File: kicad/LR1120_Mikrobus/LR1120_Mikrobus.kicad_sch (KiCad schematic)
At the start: 27 parts, among them Q1 NX2016SA-32M-EXS00A-CS06465, Q2 NT2016SA-32M-END4263A, Q3 NX3215SA, U1 LR1120, U2 SKY13588-460LF, U5 LIS2DE12, U7 M24128-BFMH6TG, U8 BGA524N6E6327XTSA1

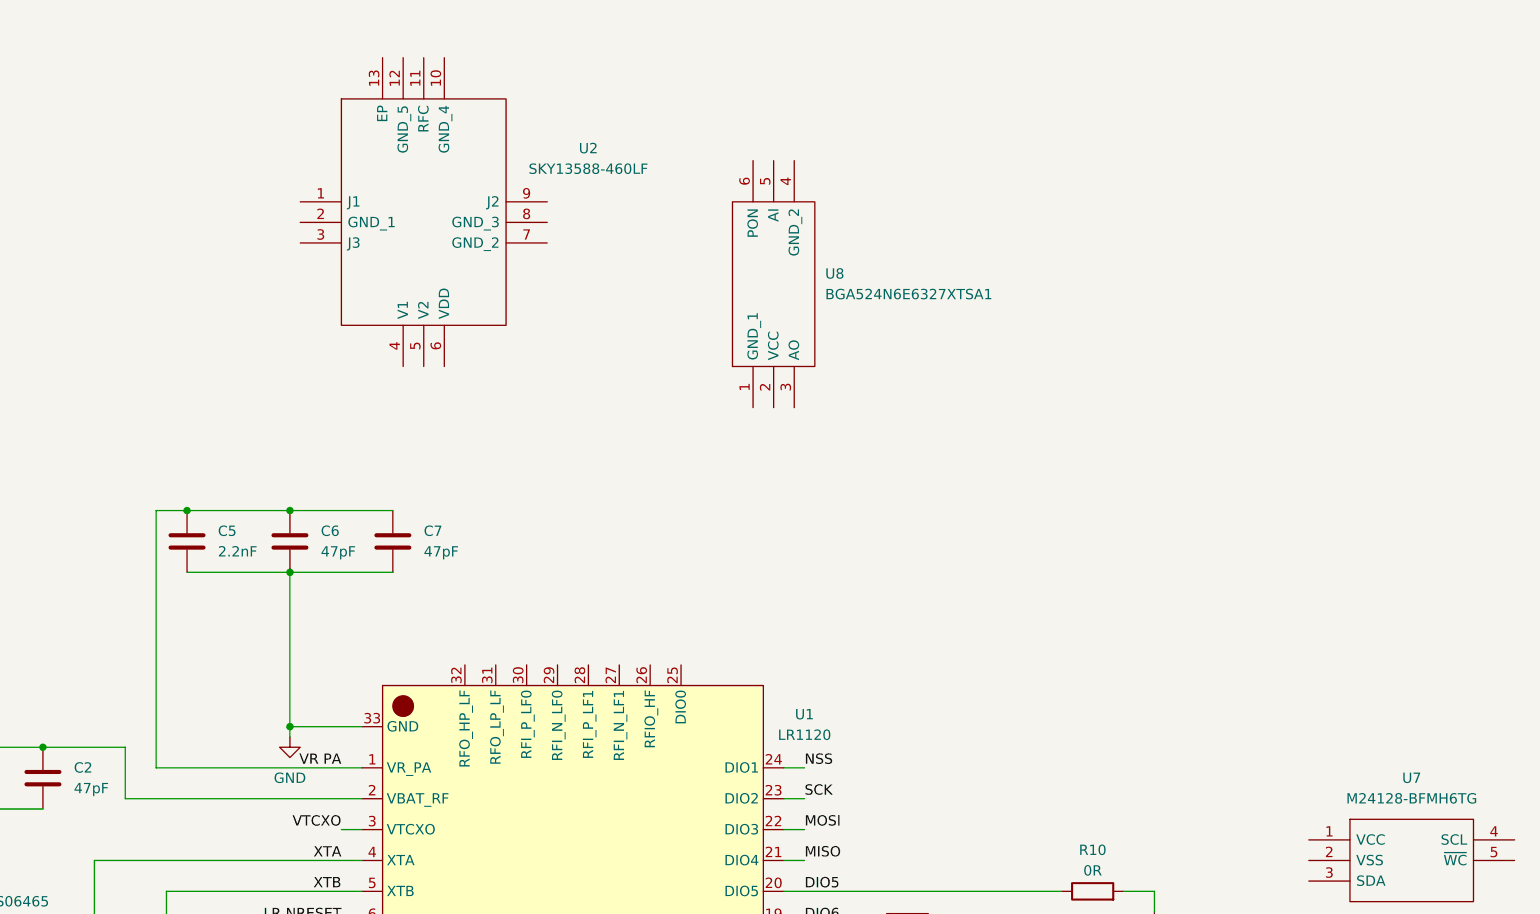
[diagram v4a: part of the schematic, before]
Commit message: added caps, inds and rclamp
Added C22-C26, C27-C28, C30, C53 and C58
Added L11-L13, L15 and L20
Added D3 (rclamp)
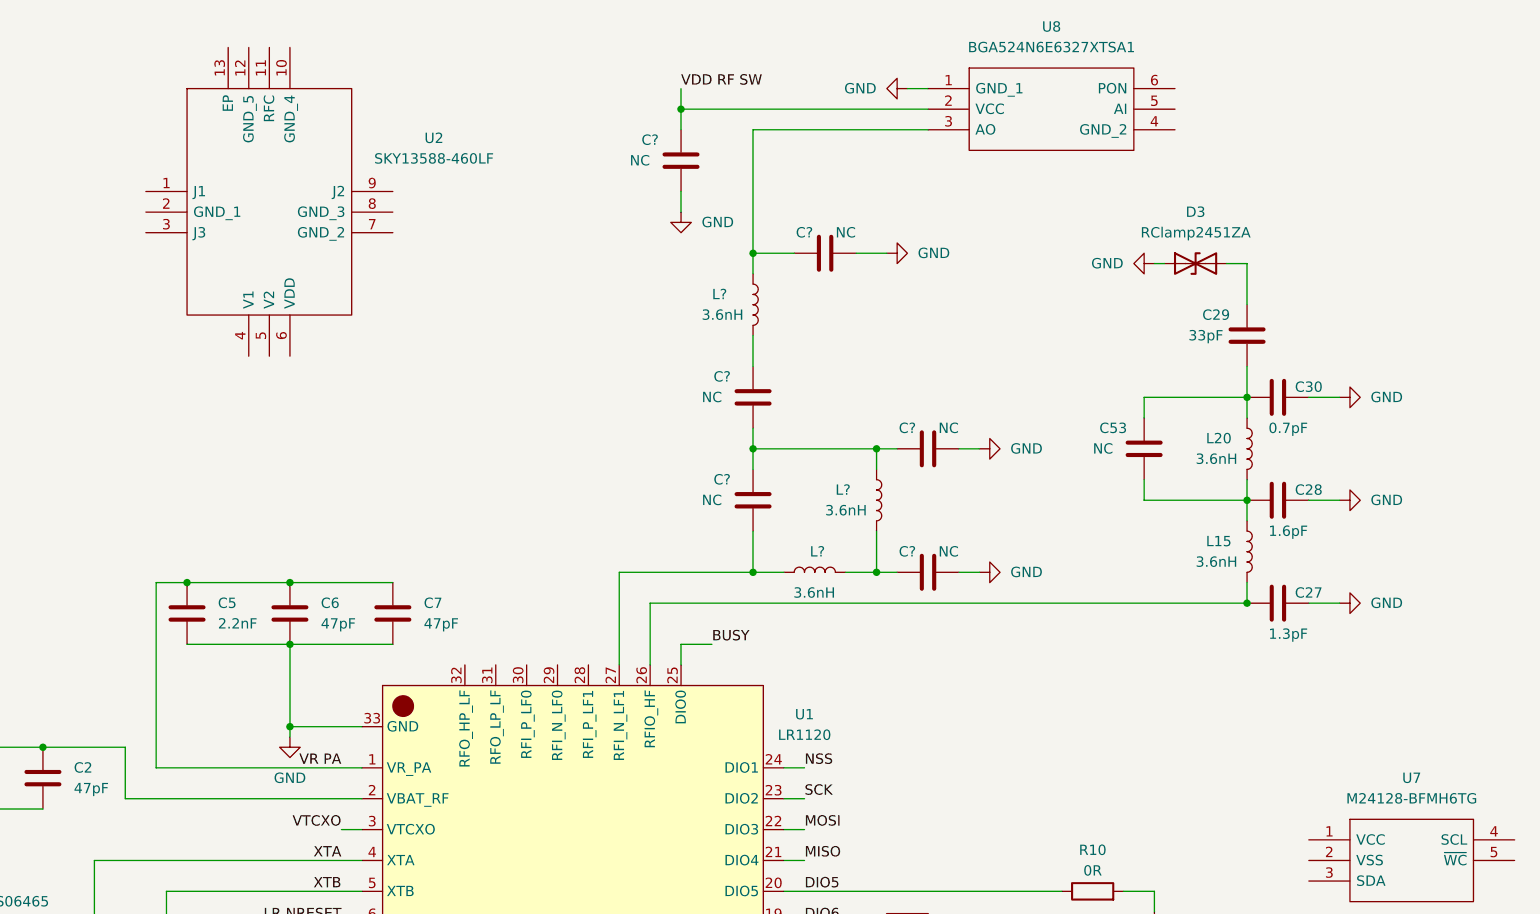
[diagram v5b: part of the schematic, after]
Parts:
- added C27: 1.3pF, Capacitor_SMD:C_01005_0402Metric, symbol Device:C
- added C28: 1.6pF, Capacitor_SMD:C_01005_0402Metric, symbol Device:C
- added C29: 33pF, Capacitor_SMD:C_01005_0402Metric, symbol Device:C
- added C30: 0.7pF, Capacitor_SMD:C_01005_0402Metric, symbol Device:C
- added C53, C? (x6): NC, Capacitor_SMD:C_01005_0402Metric, symbol Device:C
- added D3: RClamp2451ZA, Diode_SMD:D_0201_0603Metric, symbol Device:D_TVS
- added L15, L20, L? (x3): 3.6nH, Inductor_SMD:L_01005_0402Metric, symbol Device:L
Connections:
- net GND: now also U8.1 (GND_1), C27.2, C28.2, C30.2, C?.1, C?.1, C?.1, C?.1, D3.1 (A1)
- net VDD RF SW: now reaches U8.2 (VCC)
- net VDD RF SW: now also C?.2
- net at U8.3 (AO): now also C?.2, L?.1
- net BUSY: now reaches U1.25 (DIO0)
- net at U1.26 (RFIO_HF): now also C27.1, L15.2
- net at U1.27 (RFI_N_LF1): now also C?.1, L?.1
- new net: C28.1, C53.1, L15.1, L20.2
- new net: C29.1, C30.1, C53.2, L20.1
- new net: C?.1, C?.2, C?.2, L?.1
- new net: C?.2, L?.2
- new net: C?.2, L?.2, L?.2
- new net: C29.2, D3.2 (A2)
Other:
- moved on the sheet: C5, C6, C7, U2, U8

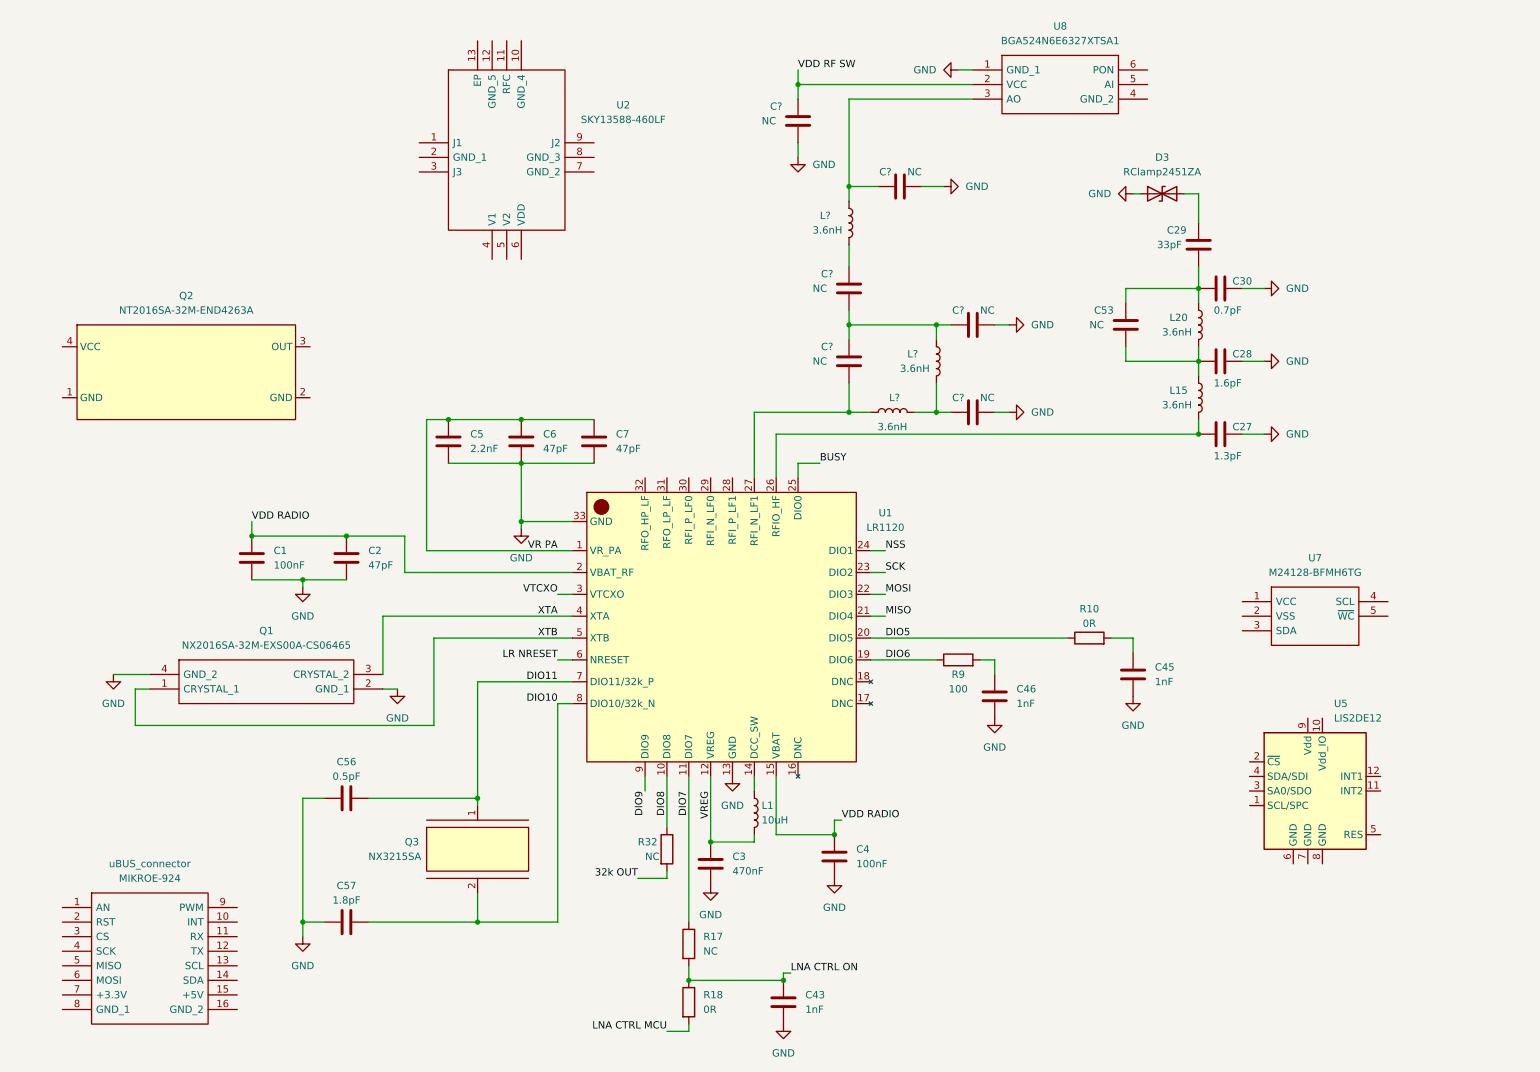
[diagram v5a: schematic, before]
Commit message: Added caps, inds and res
Adeded remaining caps, inds and res, but C47-48, C52 and R31. Some caps, inds and res need be set to the correct footprint and value.
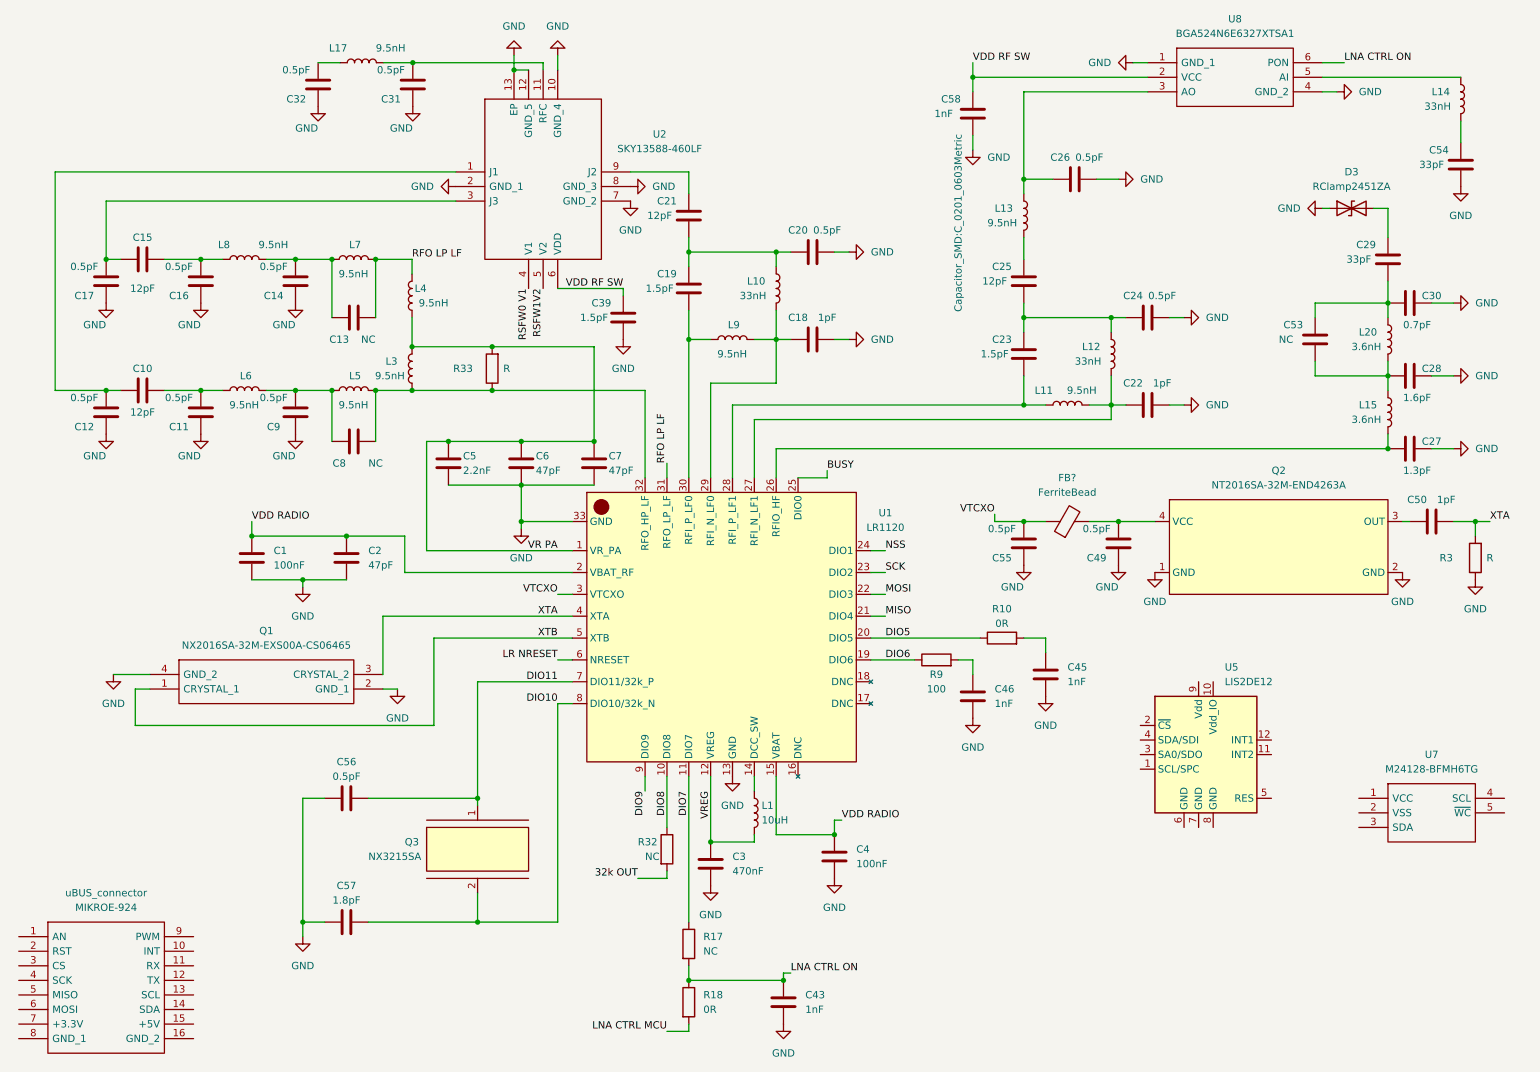
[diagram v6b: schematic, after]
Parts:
- added C10, C15, C21: 12pF, Capacitor_SMD:C_01005_0402Metric, symbol Device:C
- added C11, C12, C14, C16, C17, C20, C31, C32, C49, C55, C9: 0.5pF, Capacitor_SMD:C_01005_0402Metric, symbol Device:C
- added C13, C8: NC, Capacitor_SMD:C_01005_0402Metric, symbol Device:C
- added C18, C50: 1pF, Capacitor_SMD:C_01005_0402Metric, symbol Device:C
- added C19, C39: 1.5pF, Capacitor_SMD:C_01005_0402Metric, symbol Device:C
- added C54: 33pF, Capacitor_SMD:C_01005_0402Metric, symbol Device:C
- added FB?: FerriteBead, symbol Device:FerriteBead
- added L10, L14: 33nH, Inductor_SMD:L_01005_0402Metric, symbol Device:L
- added L17, L3, L4, L5, L6, L7, L8, L9: 9.5nH, Inductor_SMD:L_01005_0402Metric, symbol Device:L
- added R3, R33: R, symbol Device:R
- C22: renamed from C?; value NC -> 1pF
- C23: renamed from C?; value NC -> 1.5pF
- C24, C26: renamed from C?; value NC -> 0.5pF
- C25: renamed from C?; value NC -> 12pF
- C58: renamed from C?; value NC -> 1nF; footprint Capacitor_SMD:C_01005_0402Metric -> Capacitor_SMD:C_0201_0603Metric
- L11, L13: renamed from L?; value 3.6nH -> 9.5nH
- L12: renamed from L?; value 3.6nH -> 33nH
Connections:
- net GND: now also Q2.1 (GND), Q2.2 (GND), U2.10 (GND_4), U2.12 (GND_5), U2.13 (EP), U2.2 (GND_1), U2.7 (GND_2), U2.8 (GND_3), U8.4 (GND_2), C11.2, C12.2, C14.2, C16.2, C17.2, C18.1, C20.1, C31.2, C32.2, C39.1, C49.2, C54.1, C55.2, C9.2, R3.1
- net LNA CTRL ON: now also U8.6 (PON)
- net VDD RF SW: now also U2.6 (VDD), C39.2
- net VR PA: now also L3.2, L4.1, R33.2
- net VTCXO: now also C55.1, FB?.1
- net XTA: now also C50.1, R3.2
- net at U2.1 (J1): now also C10.2, C12.1
- net at U2.11 (RFC): now also C31.1, L17.2
- net at U2.3 (J3): now also C15.2, C17.1
- net RSFW0 V1: now reaches U2.4 (V1)
- net RSFW1V2: now reaches U2.5 (V2)
- net at U2.9 (J2): now also C21.2
- net at U8.5 (AI): now also L14.1
- net at C22.2, L11.2, L12.2: now also U1.27 (RFI_N_LF1)
- net at Q2.3 (OUT): now also C50.2
- net at Q2.4 (VCC): now also C49.1, FB?.2
- net at C23.1, L11.1: now also U1.28 (RFI_P_LF1); no longer U1.27 (RFI_N_LF1)
- net at U1.29 (RFI_N_LF0): now also C18.2, L10.2, L9.2
- net at U1.30 (RFI_P_LF0): now also C19.1, L9.1
- net RFO LP LF: now reaches U1.31 (RFO_LP_LF)
- net RFO LP LF: now also C13.1, L4.2, L7.2
- net at U1.32 (RFO_HP_LF): now also C8.1, L3.1, L5.2, R33.1
- new net: C19.2, C20.2, C21.1, L10.1
- new net: C8.2, C9.1, L5.1, L6.2
- new net: C54.2, L14.2
- new net: C32.1, L17.1
- new net: C15.1, C16.1, L8.1
- new net: C13.2, C14.1, L7.1, L8.2
- new net: C10.1, C11.1, L6.1
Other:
- moved on the sheet: C22, C23, C24, C25, C26, C27, C28, C29, C30, C45, C46, C5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

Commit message: Added all comp, except connectors
Added almost all components. Still remains to be placed the microbus connector and the associated caps, res and switches
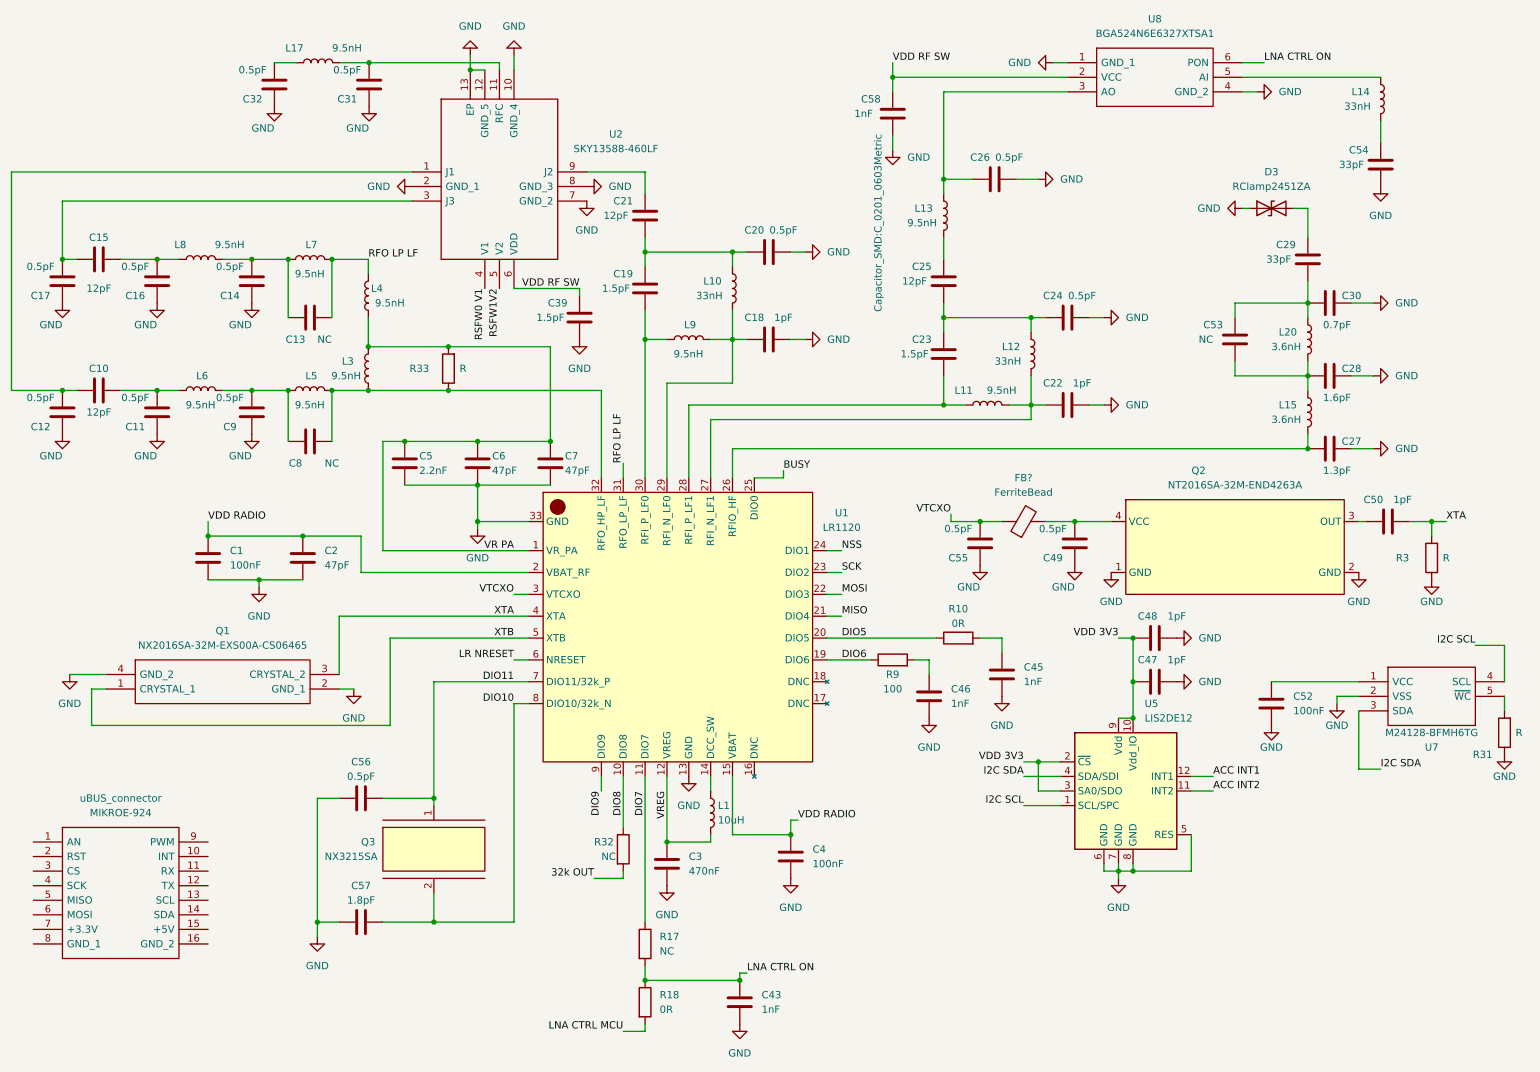
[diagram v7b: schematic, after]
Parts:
- added C47, C48: 1pF, Capacitor_SMD:C_01005_0402Metric, symbol Device:C
- added C52: 100nF, Capacitor_SMD:C_0201_0603Metric, symbol Device:C
- added R31: R, symbol Device:R
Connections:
- net GND: now also U5.5 (RES), U5.6 (GND), U5.7 (GND), U5.8 (GND), U7.2 (VSS), C47.1, C48.1, C52.2, R31.1
- net I2C SCL: now reaches U5.1 (SCL/SPC)
- net I2C SCL: now also U7.4 (SCL)
- net VDD 3V3: now reaches U5.10 (Vdd_IO)
- net VDD 3V3: now also U5.2 (~{CS}), U5.3 (SA0/SDO), U5.9 (Vdd), C47.2, C48.2
- net ACC INT2: now reaches U5.11 (INT2)
- net ACC INT1: now reaches U5.12 (INT1)
- net I2C SDA: now reaches U5.4 (SDA/SDI)
- net I2C SDA: now also U7.3 (SDA)
- net at U7.1 (VCC): now also C52.1
- net at U7.5 (~{WC}): now also R31.2
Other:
- moved on the sheet: C1, C10, C11, C12, C13, C14, C15, C16, C17, C18, C19, C2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
